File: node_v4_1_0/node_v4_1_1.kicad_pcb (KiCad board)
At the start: 4 copper layers, 45.7 x 76.2 mm, 104 parts, among them J1 Conn_01x02_Pin, J2 12402012E212A, J3 Conn_Coaxial, J4 Conn_02x08_Odd_Even, J5 Conn_02x02_Odd_Even, J6 GNSS_ANT, J7 RF_ANT, J8 Conn_01x02_Pin, J9 Conn_Coaxial, Q1 DMG2301L, Q2 DMG2301L, U1 RP2040, U10 MCP7940 / DS1307 / PCF8523, U11 1042240820, U12 CAT24M01W, U13 MAX31342EWA+T, U2 W25Q128JVS, U3 AP2112K-3.3, U4 CAT3200-5, U5 MCP73831-2-OT, U6 RFM69HCW, U7 PTS526 SK15 SMTR2 LFS, U8 PTS526 SK15 SMTR2 LFS, U9 SIM7080G

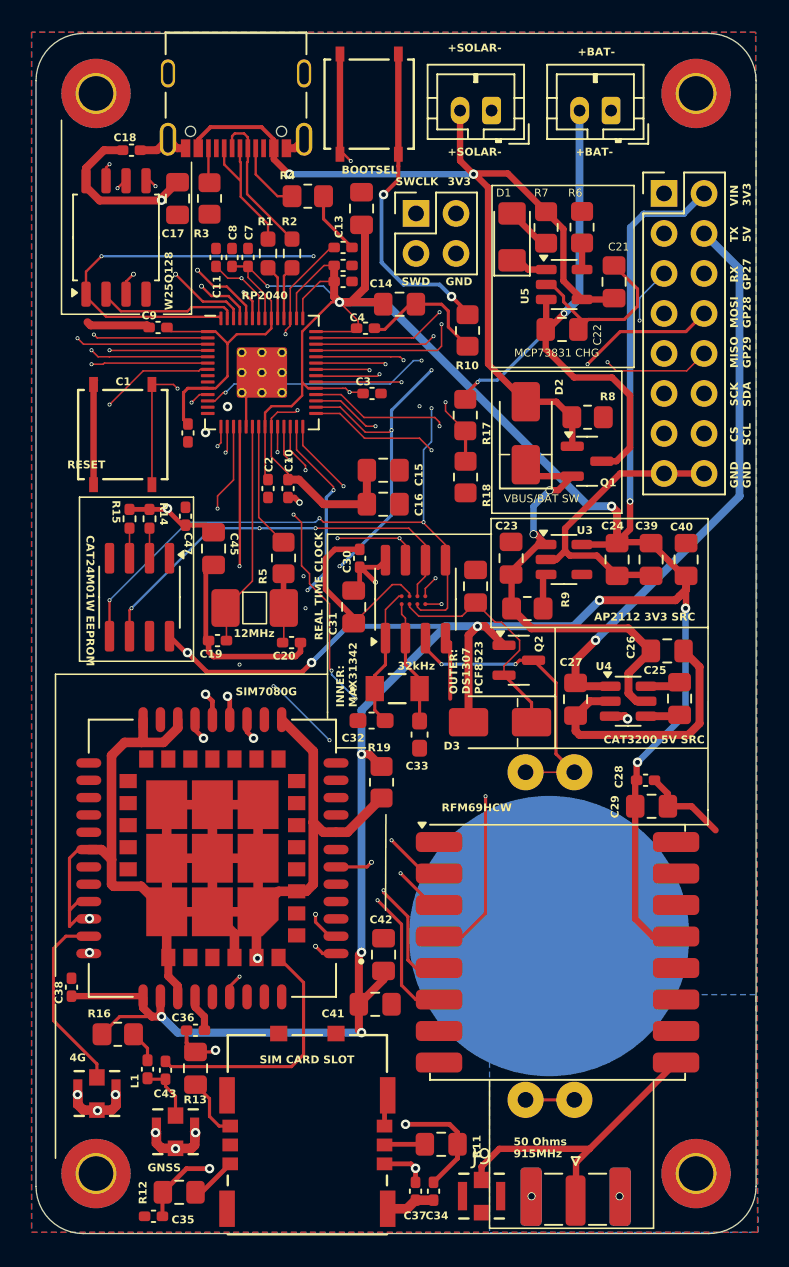
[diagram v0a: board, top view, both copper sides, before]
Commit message: small changes to 4.1.1 routing
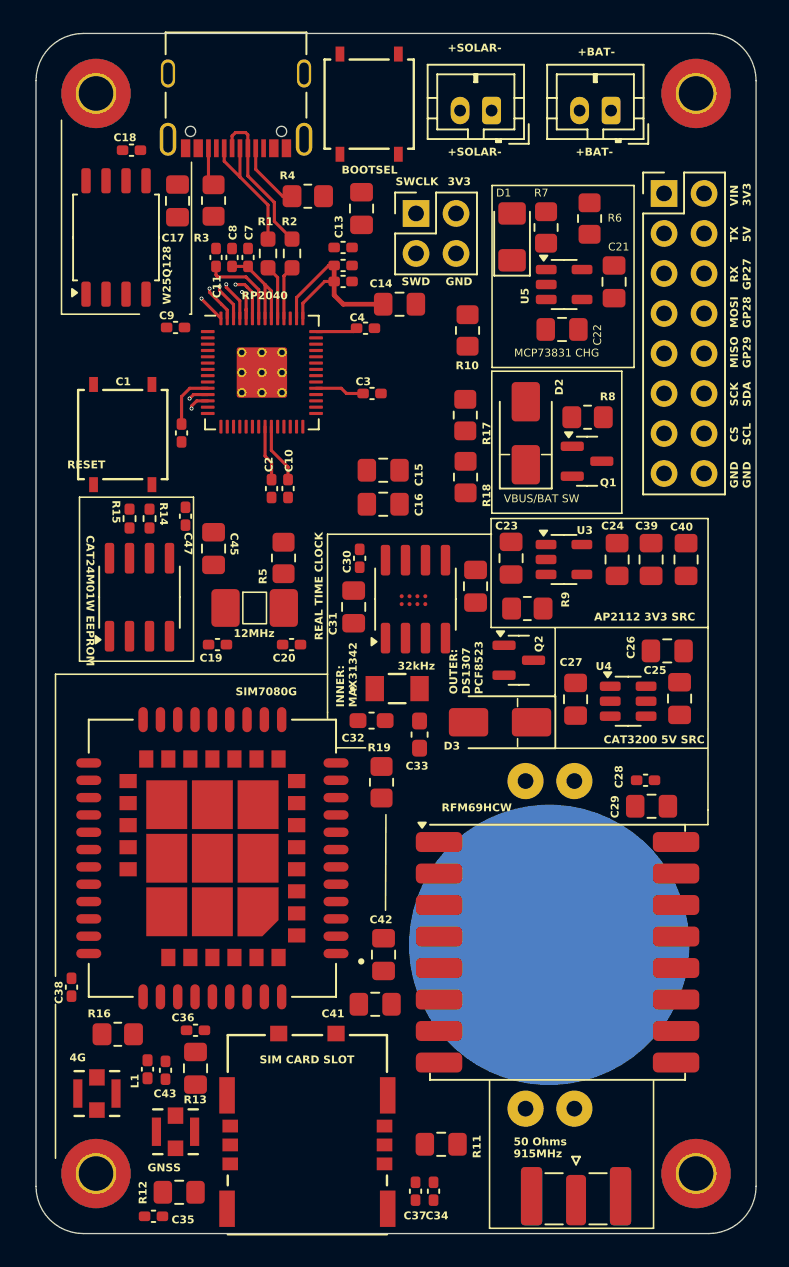
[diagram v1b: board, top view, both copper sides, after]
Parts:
- removed the G*** at (44.8, 50.4)
- removed J9: Conn_Coaxial, WiSDOM:CONN_CONMHF1-SMD_LNX
- added G***: LOGO, WiSDOM:prince, B.Cu at (42.0, 55.5)
- moved G*** 16.9 mm to (48.9, 56.2)
- moved R15 1.27 mm to (31.2, 60.6)
- moved R14 1.27 mm to (30.0, 60.6)
- moved C9 1.11 mm to (32.9, 48.4)
- moved R6 0.73 mm to (59.2, 41.5)
- moved BT1 0.56 mm to (56.6, 87.6)
- moved C1 0.41 mm to (33.3, 55.1)
- moved R3 0.29 mm to (35.3, 40.4)
- moved C19 0.25 mm to (35.6, 68.6)
- moved C2 0.22 mm to (39.0, 58.7)
- moved C17 0.15 mm to (33.0, 40.4), turned to 90 degrees
- moved C20 0.13 mm to (40.3, 68.6)
- turned C40 to -90 degrees
- turned U12 to 90 degrees
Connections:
- net RFM_ANT renamed /PERIPHERALS/ANT
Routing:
- net +3.3V: track 345.3 -> 33.3 mm, vias 18 -> 0
- net GND: track 234.9 -> 0.00 mm, vias 14 -> 0
- net SDA: track 84.2 -> 0.00 mm, vias 5 -> 0
- net SCL: track 74.5 -> 0.00 mm, vias 4 -> 0
- net VBUS: track 72.9 -> 0.00 mm, vias 2 -> 0
- net SPI_CK: track 61.7 -> 0.00 mm, vias 3 -> 0
- net MOSI: track 61.0 -> 0.00 mm, vias 4 -> 0
- net MISO: track 59.1 -> 0.00 mm, vias 3 -> 0
- net RX0: track 54.9 -> 0.00 mm, vias 2 -> 0
- net TX0: track 52.8 -> 0.00 mm, vias 2 -> 0
- net RFM_RST: track 48.2 -> 0.00 mm, vias 3 -> 0
- net RTC_BAT: track 43.2 -> 0.00 mm, vias 2 -> 0
- net /PERIPHERALS/SIM_RST: track 42.1 -> 0.00 mm, vias 2 -> 0
- net RFM_CS: track 40.8 -> 0.00 mm, vias 3 -> 0
- net 5V_CTRL: track 39.9 -> 0.00 mm, vias 5 -> 0
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- added copper zone on In2.Cu, net +3.3V
- added copper zone on In1.Cu, net GND
- removed copper zone on B.Cu, net GND
- removed copper zone on F.Cu, net GND
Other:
- board text added: "Design by Amelia Vlahogiannis 2024"
- board text added: "WiSDOM Node Version 4.0 Design Rev. 3 With Cellular"
- board text removed: "Designed by Amelia Vlahogiannis Aug. 2024"
- board text removed: "WiSDOM Node Version 4.1 Design Rev. 1 With Cellular"
